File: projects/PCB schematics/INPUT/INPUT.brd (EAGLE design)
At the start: 160 x 100 mm, 100 parts, among them IC1 OP11D, IC10 74AHC1G32DCK, IC11 OP11D, IC13 OP11D, IC14 74AHC1G32DCK, IC17 OP11D, IC18 74AHC1G32DCK, IC19 OP11D, IC2 OP11D, IC20 OP11D, IC3 OP11D, IC4 OP11D, IC5 OP11D, IC6 74AHC1G32DCK, IC7 OP11D, IC8 OP11D, IC9 74AHC1G32DCK

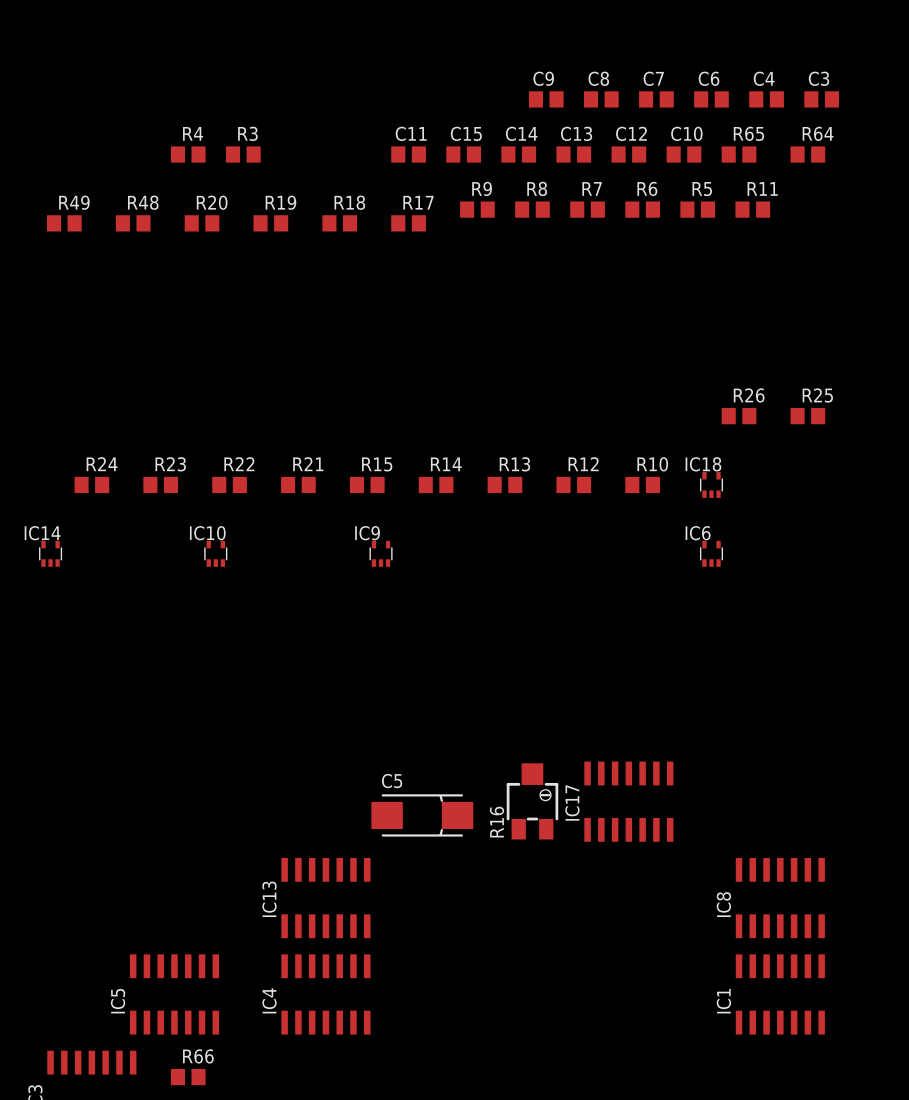
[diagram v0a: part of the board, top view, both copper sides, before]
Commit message: PROJ - Added IMD, OUTPUT.
Additional changes made to INPUT.
OUTPUT board added for ECU/motor controller signal processing.
IMD added for IMD fuse board. Rules may require fusing IMD. Might as well.
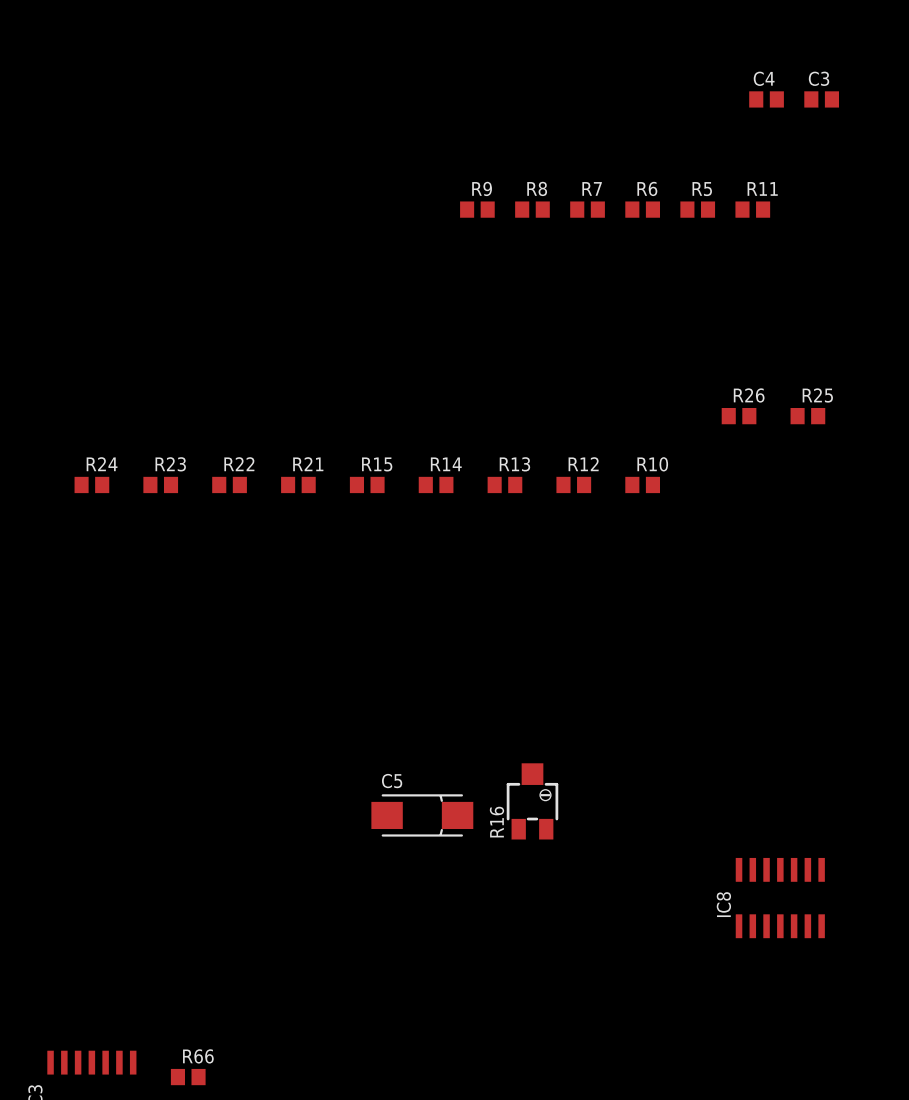
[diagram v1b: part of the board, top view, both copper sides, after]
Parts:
- removed C10, C11, C12, C13, C14, C15, C6, C7, C8, C9: (no value), rcl:C0805
- removed IC1, IC13, IC17, IC4, IC5: OP11D, linear:SO14
- removed IC10, IC14, IC18, IC6, IC9: 74AHC1G32DCK, 74xx-little-de:SC70-5
- removed R17, R18, R19, R20, R3, R4, R48, R49, R64, R65: (no value), rcl:R0805
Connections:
- removed net APPS1PLAUS: IC10.4
- removed net APPS2PLAUS: IC6.4
- removed net BOTSPLAUS: IC9.4
- removed net HVDPLAUS: IC18.4
- removed net HVD_D: IC17.6
- removed net INTERTIAPLAUS: IC14.4
- removed net INTERTIA_P: IC13.3, IC13.6
- removed net N$12: C6.1, IC5.10, R17.2
- removed net N$13: C7.1, IC5.12, R18.2
- removed net N$14: IC5.7, R18.1
- removed net N$15: IC1.1, R3.1
- removed net N$16: C10.1, IC1.10, R3.2
- removed net N$17: C11.1, IC1.12, R4.2
- removed net N$18: IC1.7, R4.1
- removed net N$20: C8.1, IC4.10, R19.2
- removed net N$23: C9.1, IC4.12, R20.2
- removed net N$24: IC4.7, R20.1
- removed net N$26: IC1.8, IC6.1
- removed net N$27: IC1.14, IC6.2
- removed net N$3: IC4.1, R19.1
- removed net N$34: IC4.8, IC9.1
- removed net N$35: IC4.14, IC9.2
- removed net N$42: IC13.1, R48.1
- removed net N$43: C12.1, IC13.10, R48.2
- removed net N$46: IC10.1, IC5.8
- removed net N$47: IC10.2, IC5.14
- removed net N$48: C13.1, IC13.12, R49.2
- removed net N$49: IC13.7, R49.1
- removed net N$50: IC13.8, IC14.1
- removed net N$51: IC13.14, IC14.2
- removed net N$6: IC5.1, R17.1
- removed net N$60: IC17.1, R64.1
- removed net N$61: C14.1, IC17.10, R64.2
- removed net N$62: C15.1, IC17.12, R65.2
- removed net N$63: IC17.7, R65.1
- removed net N$64: IC17.8, IC18.1
- removed net N$65: IC17.14, IC18.2
- removed net TIMETHRESH: IC1.13, IC1.9, IC13.13, IC13.9, IC17.13, IC17.9, IC4.13, IC4.9, IC5.13, IC5.9
- removed net VCC: IC10.5, IC14.5, IC18.5, IC6.5, IC9.5
- net +0.5V: no longer IC1.5, IC13.5, IC17.5, IC4.5, IC5.5
- net +4.5V: no longer IC1.2, IC13.2, IC17.2, IC4.2, IC5.2
- net APPS1_P: no longer IC5.3, IC5.6
- net APPS2_P: no longer IC1.3, IC1.6
- net BOTS_P: no longer IC4.3, IC4.6
- net GND: no longer C10.2, C11.2, C12.2, C13.2, C14.2, C15.2, C6.2, C7.2, C8.2, C9.2, IC10.3, IC14.3, IC18.3, IC6.3, IC9.3
- net HVD_P: no longer IC17.3
- net V+: no longer IC1.4, IC13.4, IC17.4, IC4.4, IC5.4
- net V-: no longer IC1.11, IC13.11, IC17.11, IC4.11, IC5.11
